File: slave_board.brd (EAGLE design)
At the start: 198.8 x 99.4 mm, 159 parts, among them IC3 ATMEGA2560-16AU, J11 1935161, J17 RJ45, J22 RJ45, J3 1935161, J6 1935161, K1 ORWH-SH-112D1F, Q1 PHB45NQ15T, Q2 PHB45NQ15T, Q3 BSS138L, Q5 BSS138L, Q7 PHB45NQ15T, Q8 IRFR9024TRPBF, U1 VNQ5E160KTR-E, U2 PCA9615, U3 INA213AIDCKT, U4 VNH7070ASTR, U5 VNH7070ASTR, U6 VNQ5E160KTR-E, U7 INA213AIDCKT, U8 LM340MP-5.0/NOPB, U9 LM340MP-5.0/NOPB, Y1 ABLS-16.000MHZ-B4-T

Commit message: board progress
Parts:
- moved TP1 117.4 mm to (16.0, 8.46)
- moved TP20 109.2 mm to (15.2, 27.6)
- moved J8 16.8 mm to (113.9, 2.90)
- moved U1 16.8 mm to (122.2, 14.3)
- moved C26 16.8 mm to (128.2, 23.6)
- moved C22 16.2 mm to (101.9, 18.8)
- moved C25 16.2 mm to (101.9, 25.2)
- moved J10 16.2 mm to (80.9, 2.95)
- moved C23 16.2 mm to (81.6, 25.2)
- moved C24 16.2 mm to (81.6, 18.8)
- moved J27 16.2 mm to (101.2, 2.95)
- moved U4 16.2 mm to (82.2, 12.5)
- moved U5 16.2 mm to (102.5, 12.5)
- moved C27 13.3 mm to (147.4, 26.5)
- moved U6 13.3 mm to (144.8, 14.5)
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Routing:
- net PIVOT_PWM: track 98.5 -> 78.9 mm
- net PIVOT_INB: track 93.8 -> 78.9 mm
- net V-12V_PROT: track 321.1 -> 306.6 mm
- net FROZEN1_EN: track 54.3 -> 40.9 mm
- net PIVOT_INA: track 100.5 -> 87.3 mm
- net FROZEN2_EN: track 54.9 -> 42.0 mm
- net +5V: track 457.6 -> 445.2 mm
- net FROZEN3_EN: track 55.4 -> 43.6 mm
- net ELEV_PWM: track 75.6 -> 63.8 mm
- net FROZEN4_EN: track 56.5 -> 45.4 mm
- net ELEV_INB: track 78.7 -> 68.2 mm
- net ELEV_INA: track 82.2 -> 72.7 mm
- net GND: track 467.0 -> 475.1 mm, vias 36 -> 44
- net LIQUID1_EN: track 40.3 -> 47.7 mm
- net LIQUID2_EN: track 40.4 -> 47.2 mm
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
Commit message: Resize board, add mounting holes
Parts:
- removed FD1, FD2, FD3, FD4: FIDUCIALMOUNT, SmartPrj:FIDUCIA-MOUNT
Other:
- board size 198.8 x 99.4 mm -> 200 x 100 mm
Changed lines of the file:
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@@
 <setting verticaltext="up"/>
 </settings>
-<grid distance="1" unitdist="mil" unit="mil" style="lines" multiple="1" display="no" altdistance="5" altunitdist="mil" altunit="mil"/>
+<grid distance="1" unitdist="mm" unit="mm" style="lines" multiple="1" display="no" altdistance="0.1" altunitdist="mm" altunit="mm"/>
 <layers>
 <layer number="1" name="Top" color="4" fill="1" visible="yes" active="yes"/>
@@
 <board>
 <plain>
-<wire x1="0" y1="0" x2="198.735" y2="0" width="0" layer="20"/>
-<wire x1="198.735" y1="0" x2="198.787378125" y2="99.42325625" width="0" layer="20"/>
-<wire x1="198.787378125" y1="99.42325625" x2="0" y2="99.365" width="0" layer="20"/>
+<wire x1="0" y1="0" x2="200" y2="0" width="0" layer="20"/>
+<wire x1="200" y1="0" x2="200" y2="100" width="0" layer="20"/>
+<wire x1="200" y1="100" x2="0" y2="99.365" width="0" layer="20"/>
 <wire x1="0" y1="99.365" x2="0" y2="0" width="0" layer="20"/>
+<hole x="3" y="97" drill="0.3"/>
+<hole x="197" y="97" drill="0.3"/>
+<hole x="197" y="3" drill="0.3"/>
+<hole x="3" y="3" drill="0.3"/>
 </plain>
 <attributes>
@@
 <attribute name="VALUE" x="144.2212" y="66.802" size="1.27" layer="27" rot="R270"/>
 </element>
-<element name="FD1" library="SmartPrj" package="FIDUCIA-MOUNT" value="FIDUCIALMOUNT" x="2.54" y="2.54" smashed="yes"/>
-<element name="FD2" library="SmartPrj" package="FIDUCIA-MOUNT" value="FIDUCIALMOUNT" x="2.54" y="97.155" smashed="yes"/>
-<element name="FD3" library="SmartPrj" package="FIDUCIA-MOUNT" value="FIDUCIALMOUNT" x="195.58" y="96.52" smashed="yes"/>
 <element name="C3" library="rcl" library_urn="urn:adsk.eagle:library:334" package="C0603" package3d_urn="urn:adsk.eagle:package:23616/2" value="100n" x="122.301" y="74.93" smashed="yes" rot="R180">
 <attribute name="NAME" x="123.19" y="77.47" size="1.27" layer="25" rot="R180"/>
@@
 <attribute name="SPICEPREFIX" value="C" x="118.872" y="74.549" size="1.778" layer="27" rot="R90" display="off"/>
 </element>
-<element name="FD4" library="SmartPrj" package="FIDUCIA-MOUNT" value="FIDUCIALMOUNT" x="195.58" y="3.175" smashed="yes"/>
 <element name="Y1" library="ABLS-16.000MHZ-B4-T" package="ABLS-16.000MHZ-B4-T" value="ABLS-16.000MHZ-B4-T" x="118.11" y="43.434" smashed="yes">
 <attribute name="AVAILABILITY" value="Unavailable" x="87.63" y="19.304" size="1.778" layer="27" display="off"/>
@@
 <wire x1="116.824" y1="65.135" x2="116.078" y2="64.428" width="0.3048" layer="1"/>
 <polygon width="0.127" layer="16" rank="2">
-<vertex x="198.374" y="0.254"/>
-<vertex x="0.254" y="0.254"/>
-<vertex x="0.254" y="99.06"/>
-<vertex x="198.374" y="99.06"/>
+<vertex x="203.374" y="-1.746"/>
+<vertex x="-2.746" y="-1.746"/>
+<vertex x="-2.746" y="103.06"/>
+<vertex x="203.374" y="103.06"/>
 </polygon>
 <wire x1="11.645" y1="23.495" x2="11.43" y2="23.55" width="0.254" layer="1"/>
@@
 <wire x1="18.415" y1="57.15" x2="17.78" y2="57.15" width="0" layer="19" extent="1-1"/>
 <wire x1="22.86" y1="19.685" x2="22.733" y2="19.05" width="0" layer="19" extent="1-1"/>
-<wire x1="96.774" y1="9.9314" x2="95.5944" y2="9.9964" width="0" layer="19" extent="1-1"/>
 <wire x1="80.2894" y1="14.9464" x2="77.7494" y2="14.9464" width="0" layer="19" extent="1-1"/>
 <wire x1="80.7094" y1="18.8214" x2="80.7094" y2="18.6064" width="0" layer="19" extent="1-1"/>

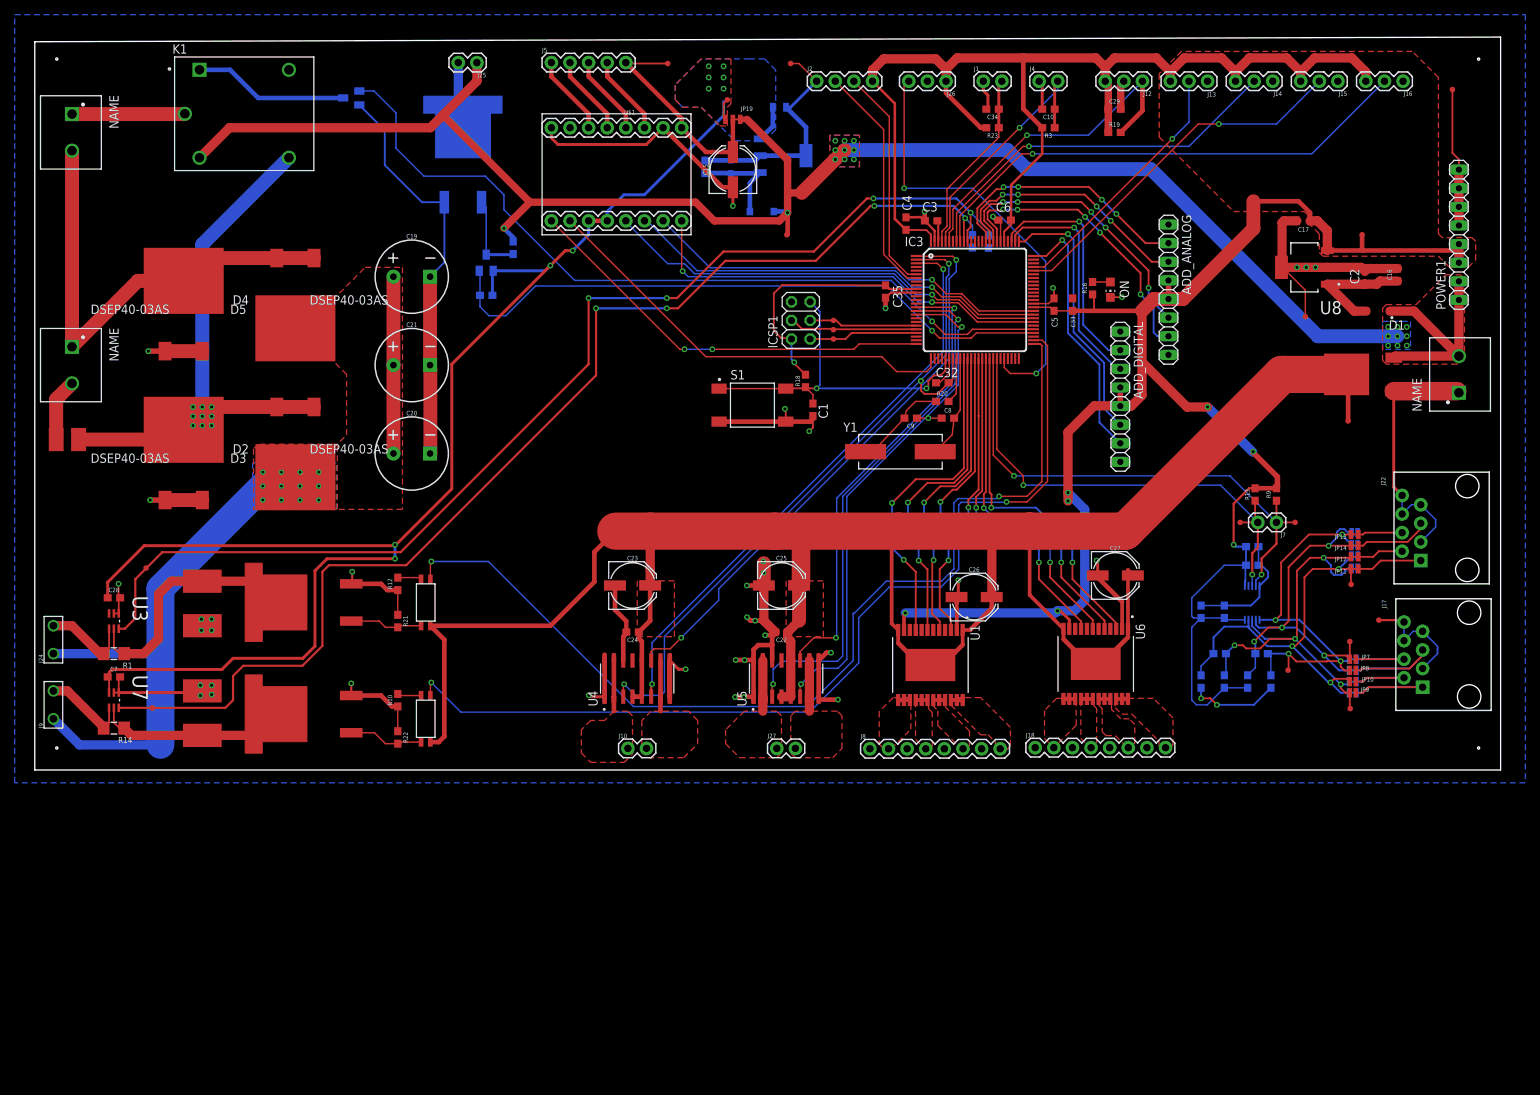
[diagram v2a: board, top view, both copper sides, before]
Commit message: Added screw terminal headers
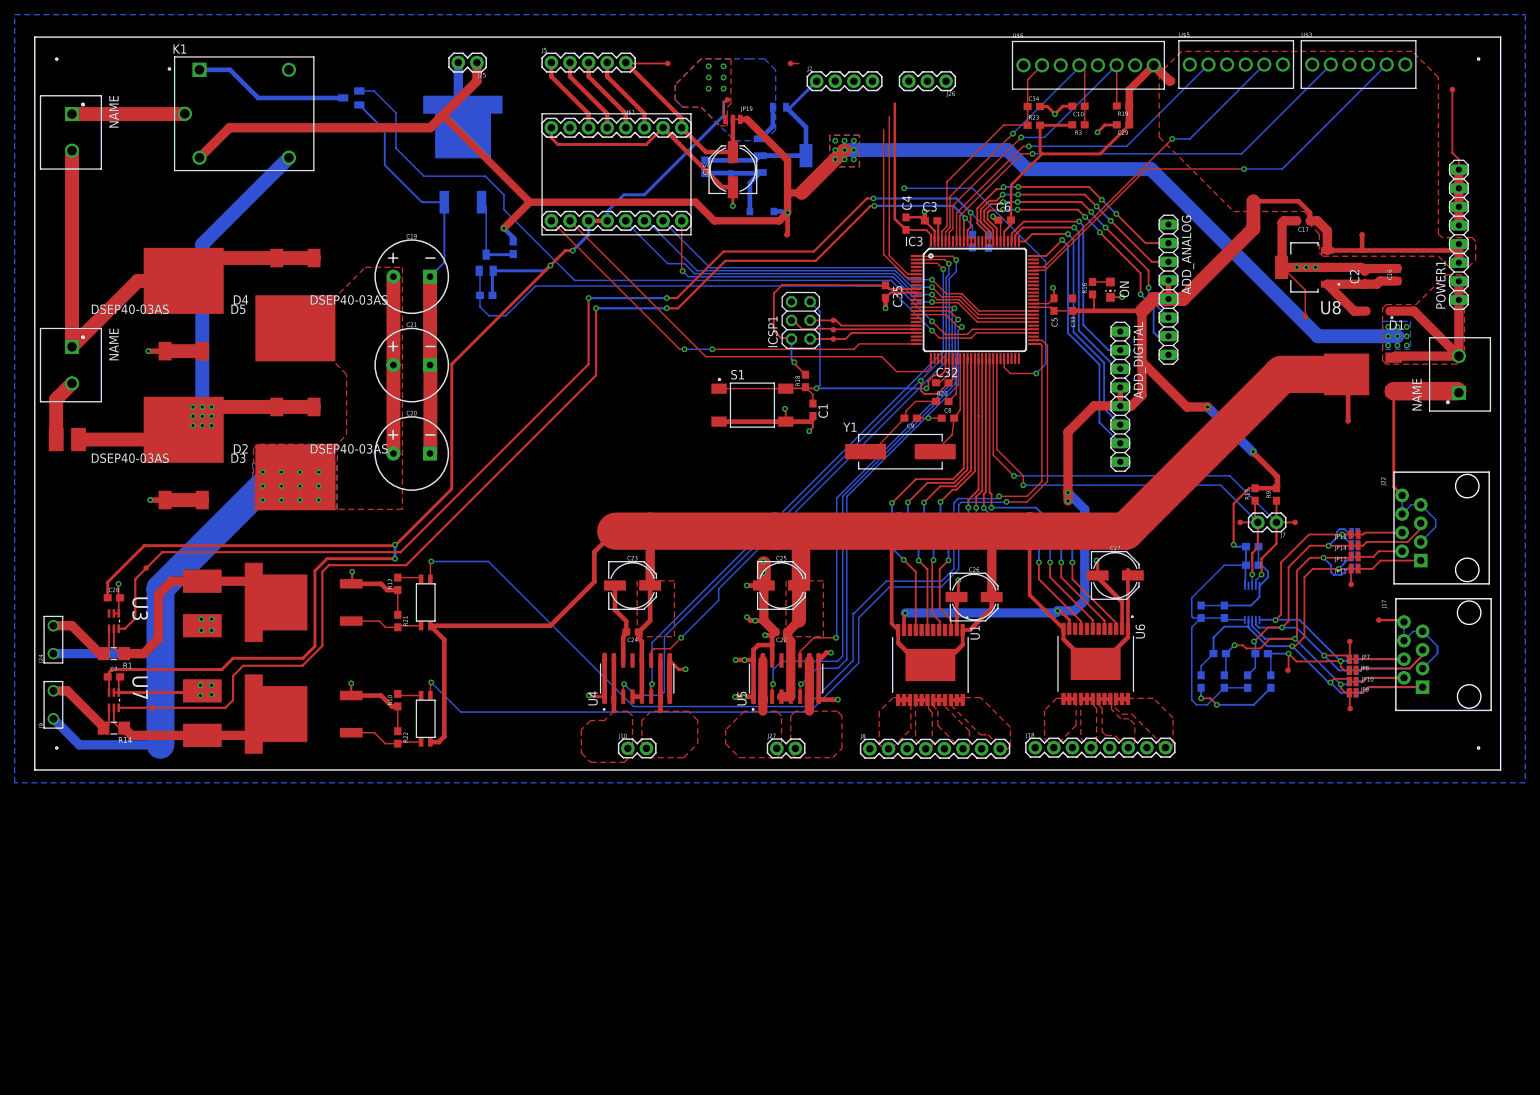
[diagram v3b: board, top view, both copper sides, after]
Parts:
- removed J1, J4: (no value), SparkFun-Connectors:1X02
- removed J12, J13, J14, J15, J16: (no value), SparkFun-Connectors:1X03
- added U$3, U$5: OSTVN06A150, smoothio:6PIN_SCREW_TERMINAL
- added U$6: OSTVN08A150, smoothio:8PIN_SCREW_TERMINAL
- moved C34 5.65 mm to (136.3, 90.5), turned to 0 degrees
- moved R23 5.64 mm to (136.3, 88.0), turned to 0 degrees
- moved R3 4.12 mm to (142.4, 88.0)
- moved C10 4.12 mm to (142.4, 90.6)
- moved R19 3.79 mm to (148.5, 90.6), turned to 180 degrees
- moved C29 2.43 mm to (148.5, 88.0), turned to 180 degrees
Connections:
- net +5V: now also U$3.P$4, U$3.P$7, U$5.P$4, U$5.P$7, U$6.P$9; no longer J12.3, J13.3, J14.3, J15.3, J16.3
- net CAROUSEL_POS: now also U$6.P$7; no longer J12.1
- net CUP_MASS0: now also U$5.P$3; no longer J14.2
- net CUP_MASS1: now also U$3.P$3; no longer J16.2
- net CUP_SENSE0: now also U$5.P$6; no longer J13.2
- net CUP_SENSE1: now also U$3.P$6; no longer J15.2
- net GND: now also U$3.P$1, U$3.P$5, U$5.P$1, U$5.P$5, U$6.P$1, U$6.P$4, U$6.P$6, U$6.P$8; no longer J1.1, J12.2, J13.1, J14.1, J15.1, J16.1, J4.1
- net THERMISTOR0: now also U$6.P$3; no longer J1.2
- net THERMISTOR1: now also U$6.P$5; no longer J4.2
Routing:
- net +5V: track 445.2 -> 359.3 mm
- net ELEV_ENC_OUT: track 60.1 -> 45.2 mm
- net CUP_SENSE1: track 49.7 -> 59.8 mm
- net PIVOT_ENC_B: track 32.1 -> 22.8 mm
- net CUP_SENSE0: track 35.0 -> 42.9 mm
- net GND: track 475.1 -> 468.1 mm, vias 44 -> 46
- net PIVOT_ENC_A: track 30.5 -> 23.7 mm
- net THERMISTOR0: track 25.2 -> 31.6 mm
- net CUP_MASS1: track 69.0 -> 62.7 mm
- net THERMISTOR1: track 34.7 -> 40.0 mm
- net CUP_MASS0: track 51.9 -> 46.6 mm
- net CAROUSEL_POS: track 45.9 -> 40.9 mm
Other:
- outline, holes or cut-outs redrawn

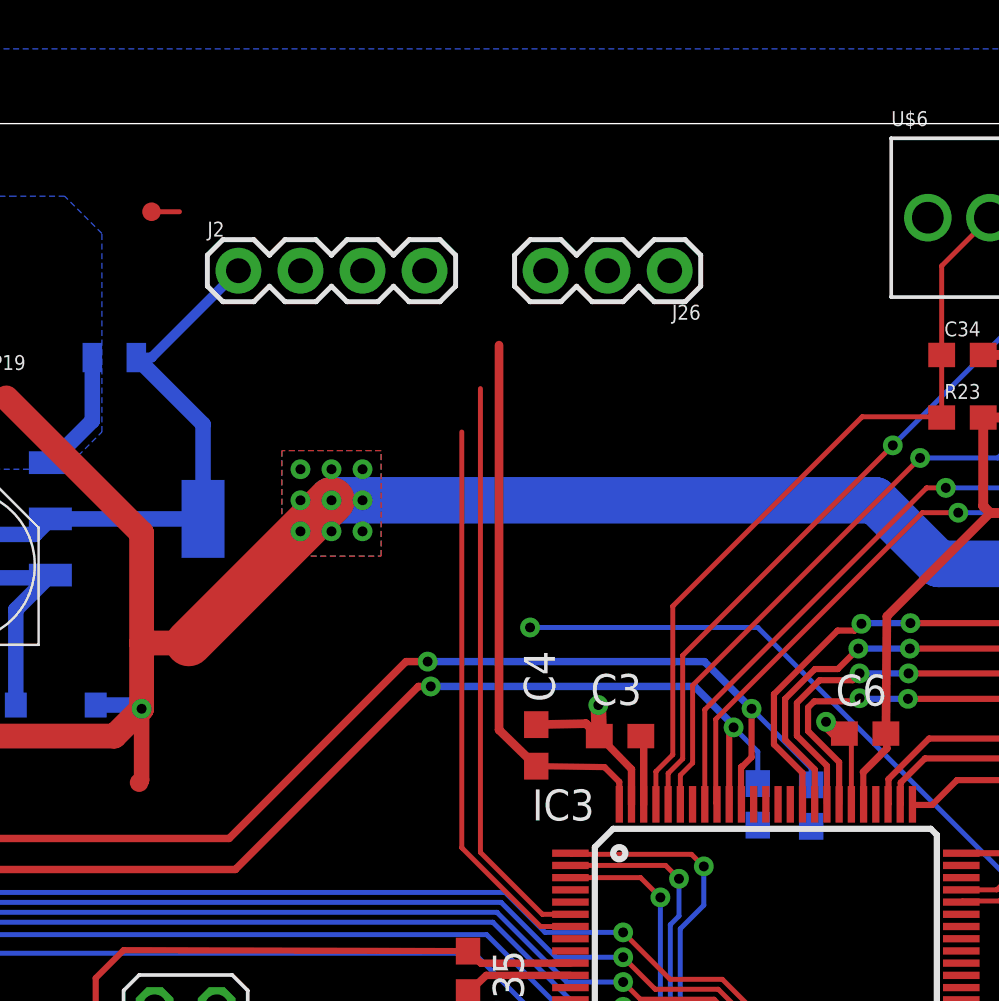
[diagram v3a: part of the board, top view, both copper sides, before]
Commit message: Placed another screw terminal
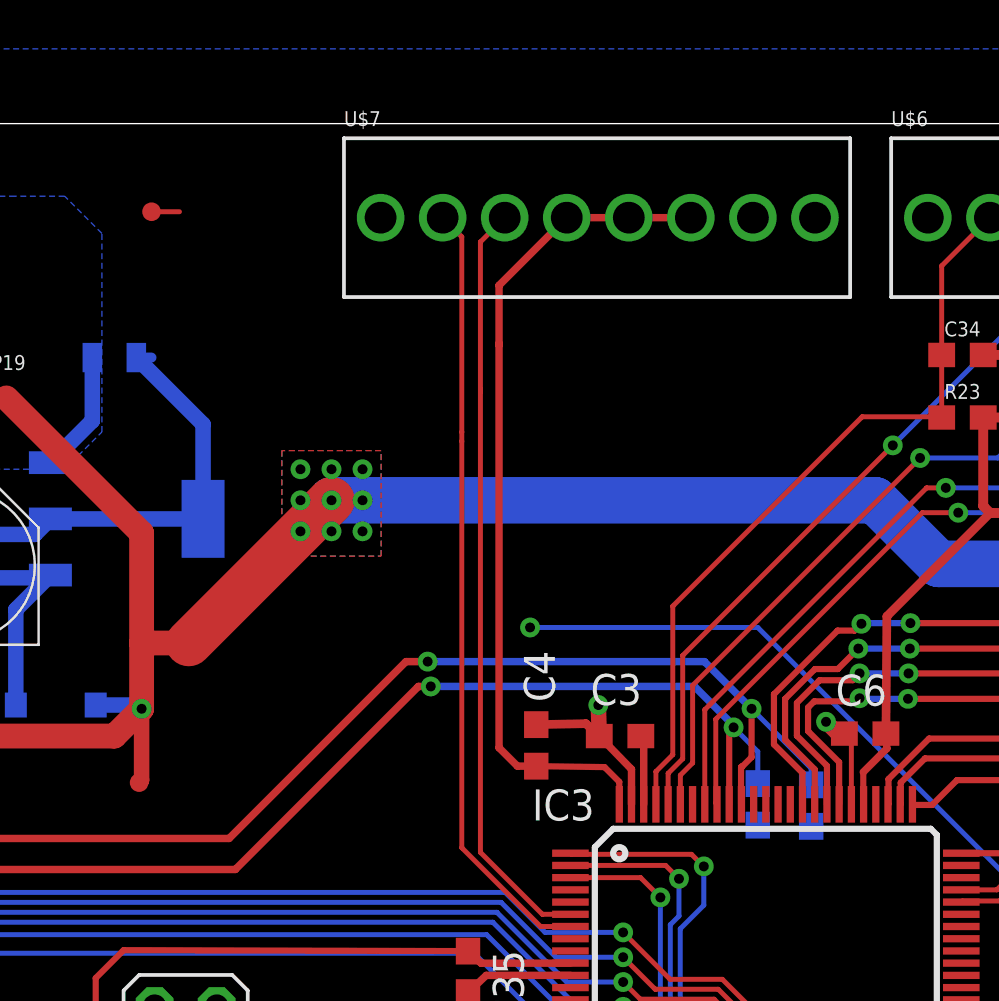
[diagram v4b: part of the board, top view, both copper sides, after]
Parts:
- removed J2: (no value), SparkFun-Connectors:1X04
- removed J26: (no value), SparkFun-Connectors:1X03
- added U$7: OSTVN08A150, smoothio:8PIN_SCREW_TERMINAL
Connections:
- net +5V: now also U$3.3, U$3.6, U$5.3, U$5.6, U$6.8, U$7.4, U$7.5, U$7.6; no longer J2.4, J26.1, U$3.P$4, U$3.P$7, U$5.P$4, U$5.P$7, U$6.P$9
- net CAROUSEL_POS: now also U$6.6; no longer U$6.P$7
- net CUP_MASS0: now also U$5.2; no longer U$5.P$3
- net CUP_MASS1: now also U$3.2; no longer U$3.P$3
- net CUP_SENSE0: now also U$5.5; no longer U$5.P$6
- net CUP_SENSE1: now also U$3.5; no longer U$3.P$6
- net ELEV_ENC_OUT: now also U$7.8; no longer J26.3
- net GND: now also U$3.1, U$3.4, U$5.1, U$5.4, U$6.1, U$6.3, U$6.5, U$6.7, U$7.1, U$7.7; no longer J2.1, J26.2, U$3.P$1, U$3.P$5, U$5.P$1, U$5.P$5, U$6.P$1, U$6.P$4, U$6.P$6, U$6.P$8
- net PIVOT_ENC_A: now also U$7.3; no longer J2.3
- net PIVOT_ENC_B: now also U$7.2; no longer J2.2
- net THERMISTOR0: now also U$6.2; no longer U$6.P$3
- net THERMISTOR1: now also U$6.4; no longer U$6.P$5
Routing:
- net +5V: track 359.3 -> 371.2 mm
- net PIVOT_ENC_B: track 22.8 -> 31.9 mm
- net PIVOT_ENC_A: track 23.7 -> 31.1 mm
- net GND: track 468.1 -> 463.1 mm
